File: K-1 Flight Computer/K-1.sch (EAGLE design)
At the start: 25 parts, among them IC1 BMP280, IC2 7805L, J1 1X2-3.5MM, J6 1X2-3.5MM, U1 MPU-6050-1, U2 W25Q32FV

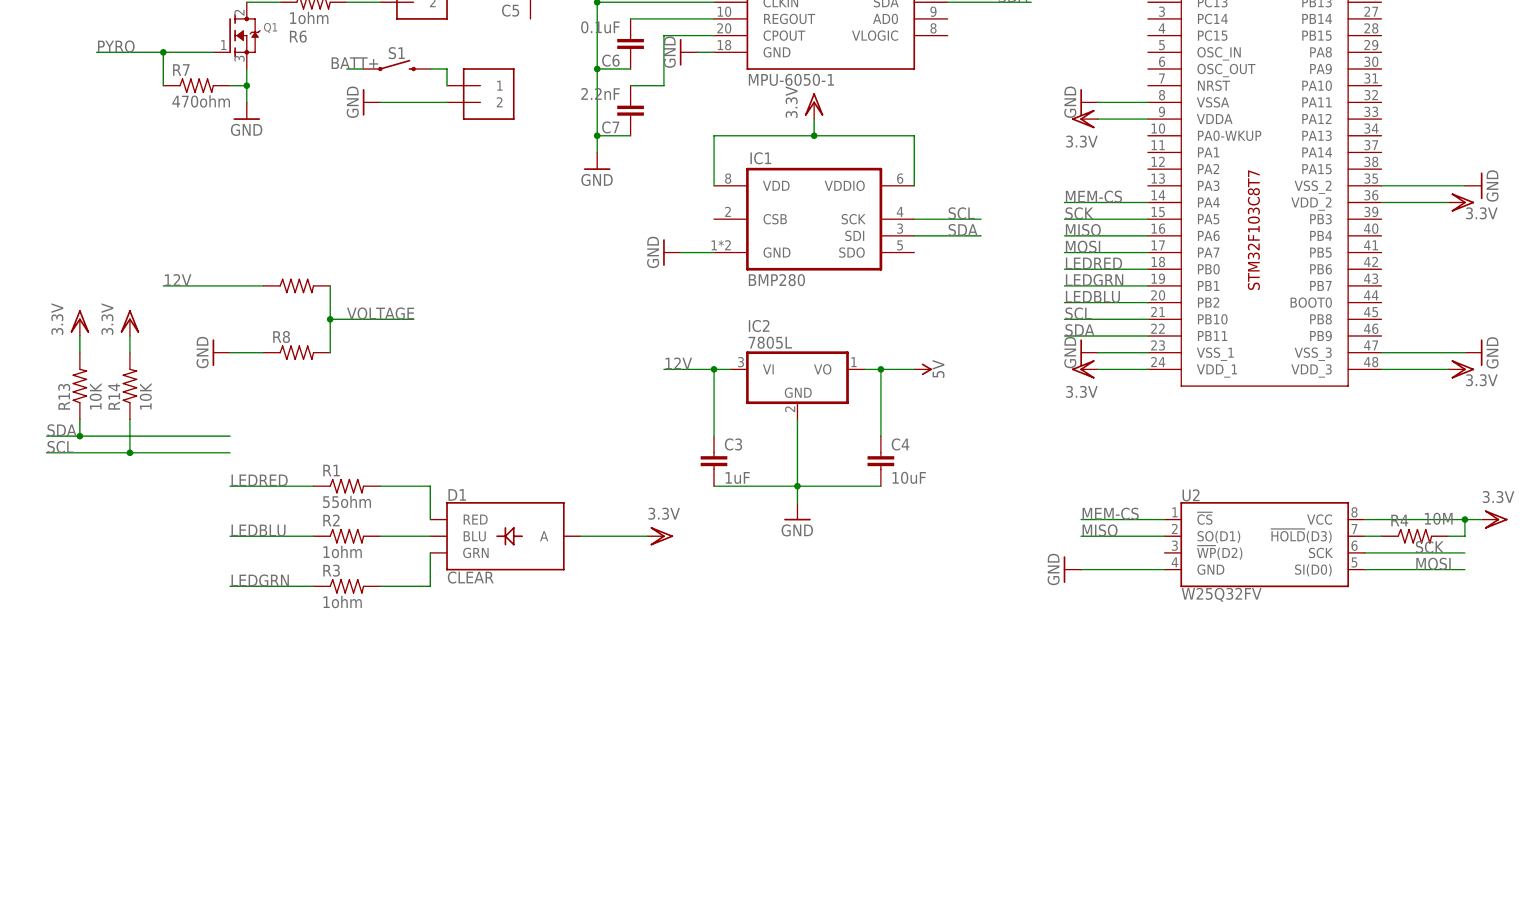
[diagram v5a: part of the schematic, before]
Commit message: completed bootloader circuit
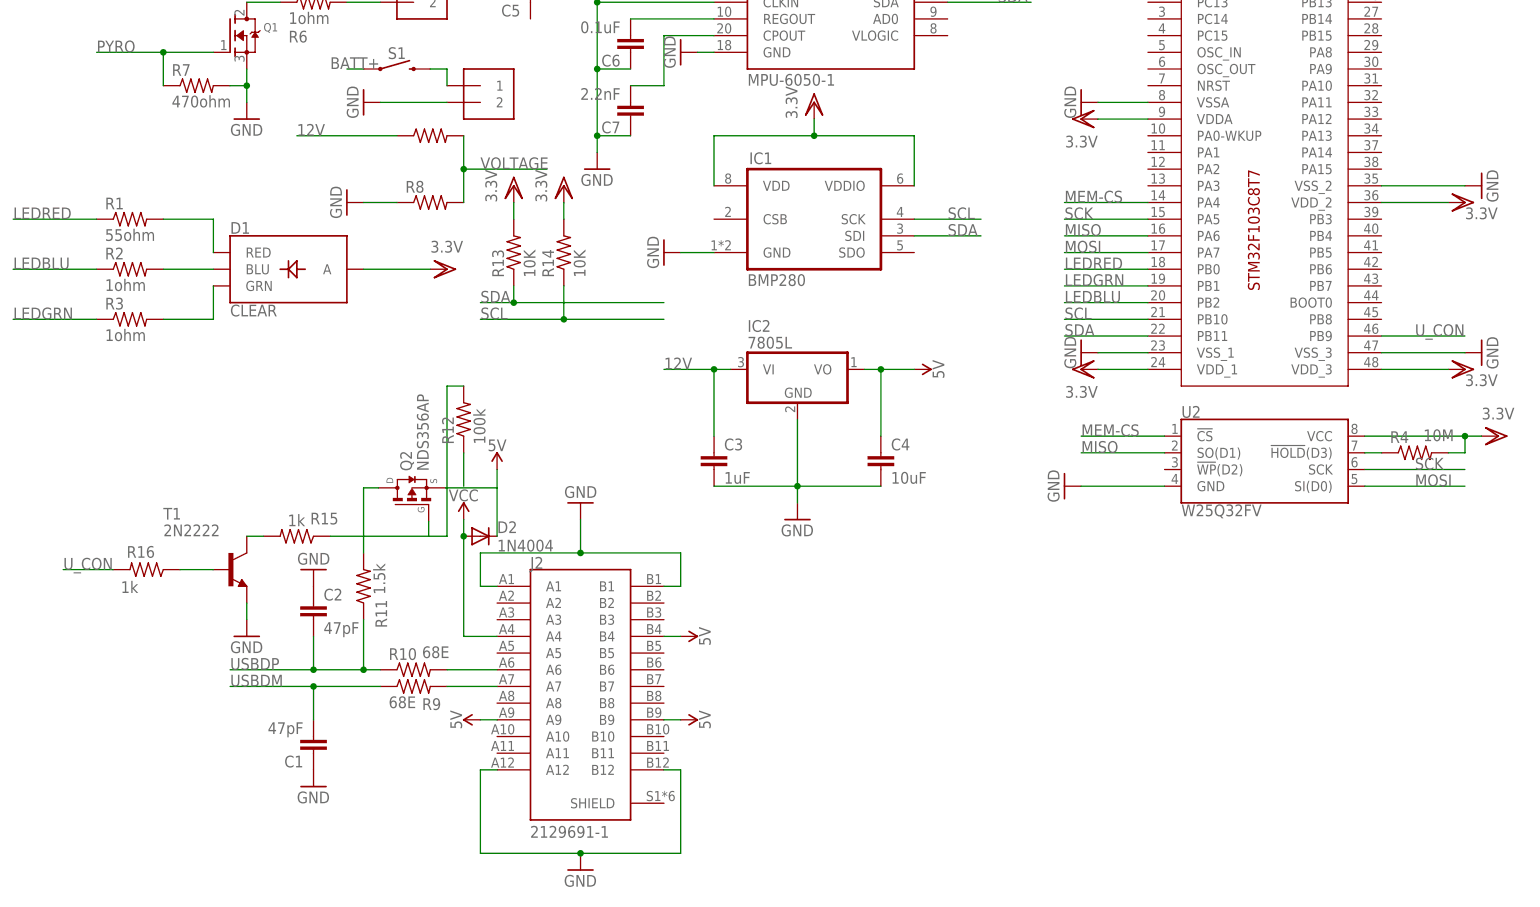
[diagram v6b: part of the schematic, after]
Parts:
- added C1, C2: 47pF, capacitor-wima:C2,5-3
- added D2: 1N4004, adafruit:1N4004
- added J2: 2129691-1, typeC:2129691-1
- added Q2: NDS356AP, NDS356AP:NDS356AP
- added R10, R9: 68E, adafruit:R-US_0204/2V
- added R11: 1.5k, adafruit:R-US_0204/2V
- added R12: 100k, adafruit:R-US_0204/2V
- added R15, R16: 1k, adafruit:R-US_0204/2V
- added T1: 2N2222, adafruit:2N2222
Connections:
- new net N$10: Q2.G, R12.2, R15.1
- new net N$13: R15.2, T1.C
- new net N$14: R16.1, T1.B
- new net N$16: J2.A7, R9.2
- new net N$7: J2.A6, R10.2
- new net N$8: Q2.D, R11.2
- new net N$9: R12.1
- new net USBDM: C1.2, R9.1
- new net USBDP: C2.2, R10.1, R11.1
- new net U_CON: R16.2, U$1.PB9
- new net VCC: D2.A, J2.A4
- net 5V: now also D2.C, J2.A9, J2.B4, J2.B9, Q2.S
- net GND: now also C1.1, C2.1, J2.A1, J2.A12, J2.B1, J2.B12, T1.E
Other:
- moved on the sheet: D1, R1, R13, R14, R2, R3, R4, R8, U2

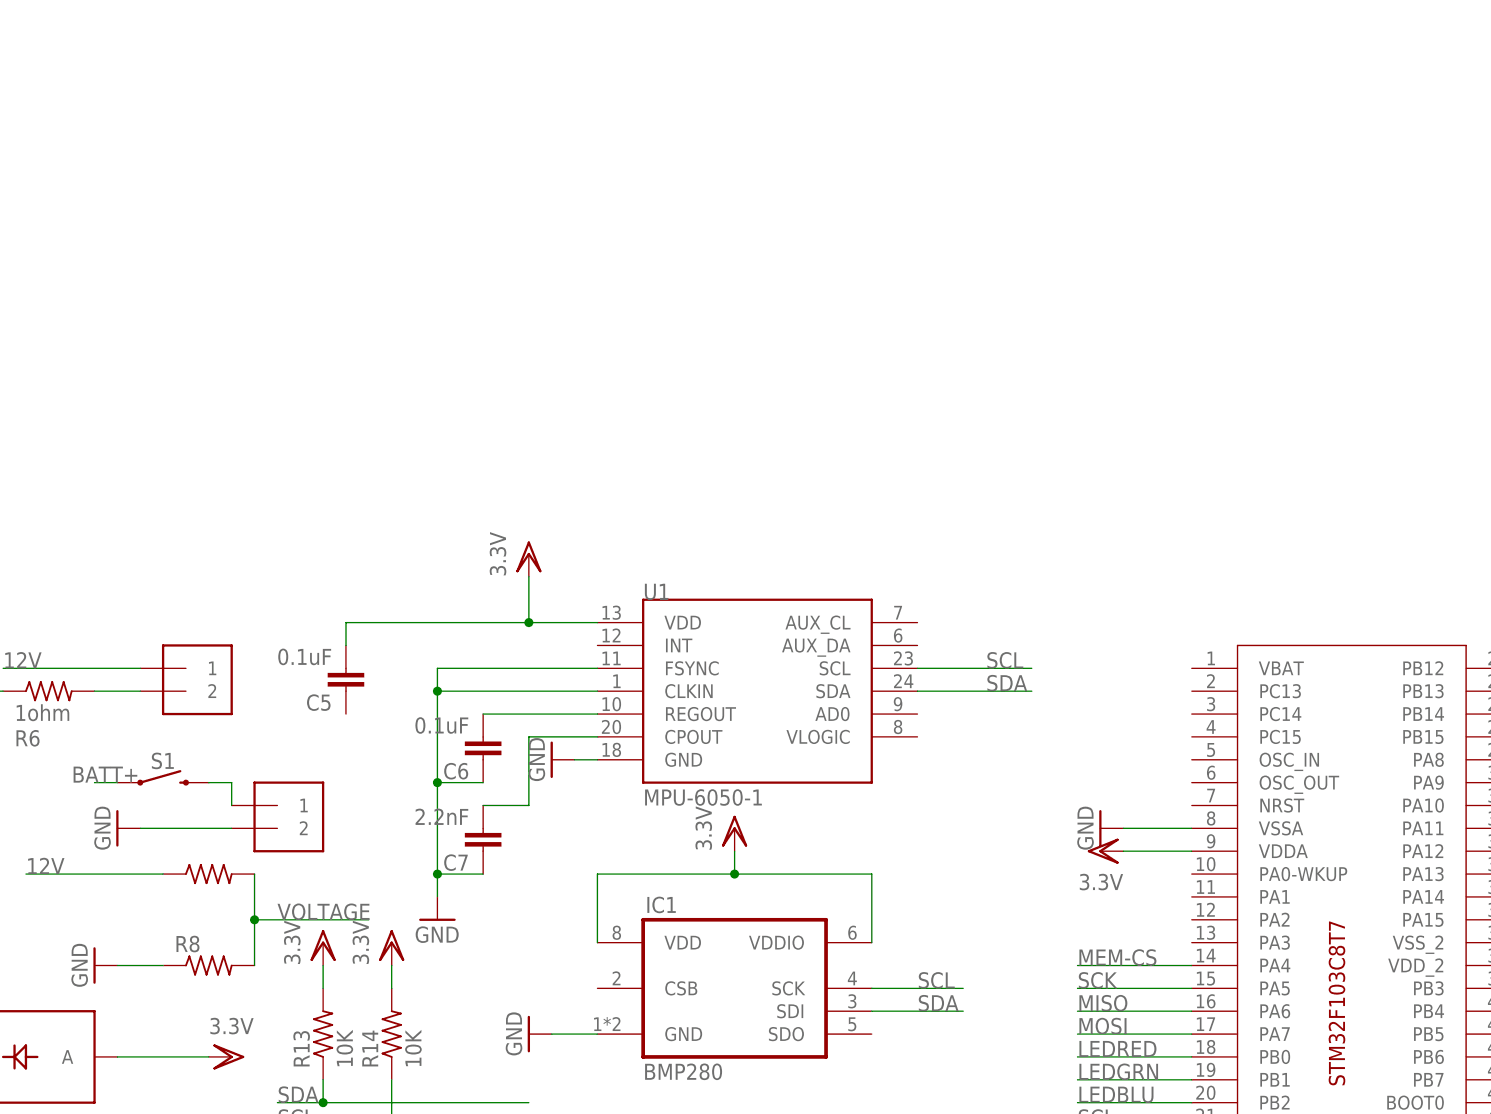
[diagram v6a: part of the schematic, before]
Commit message: completed IMU breakout circuit
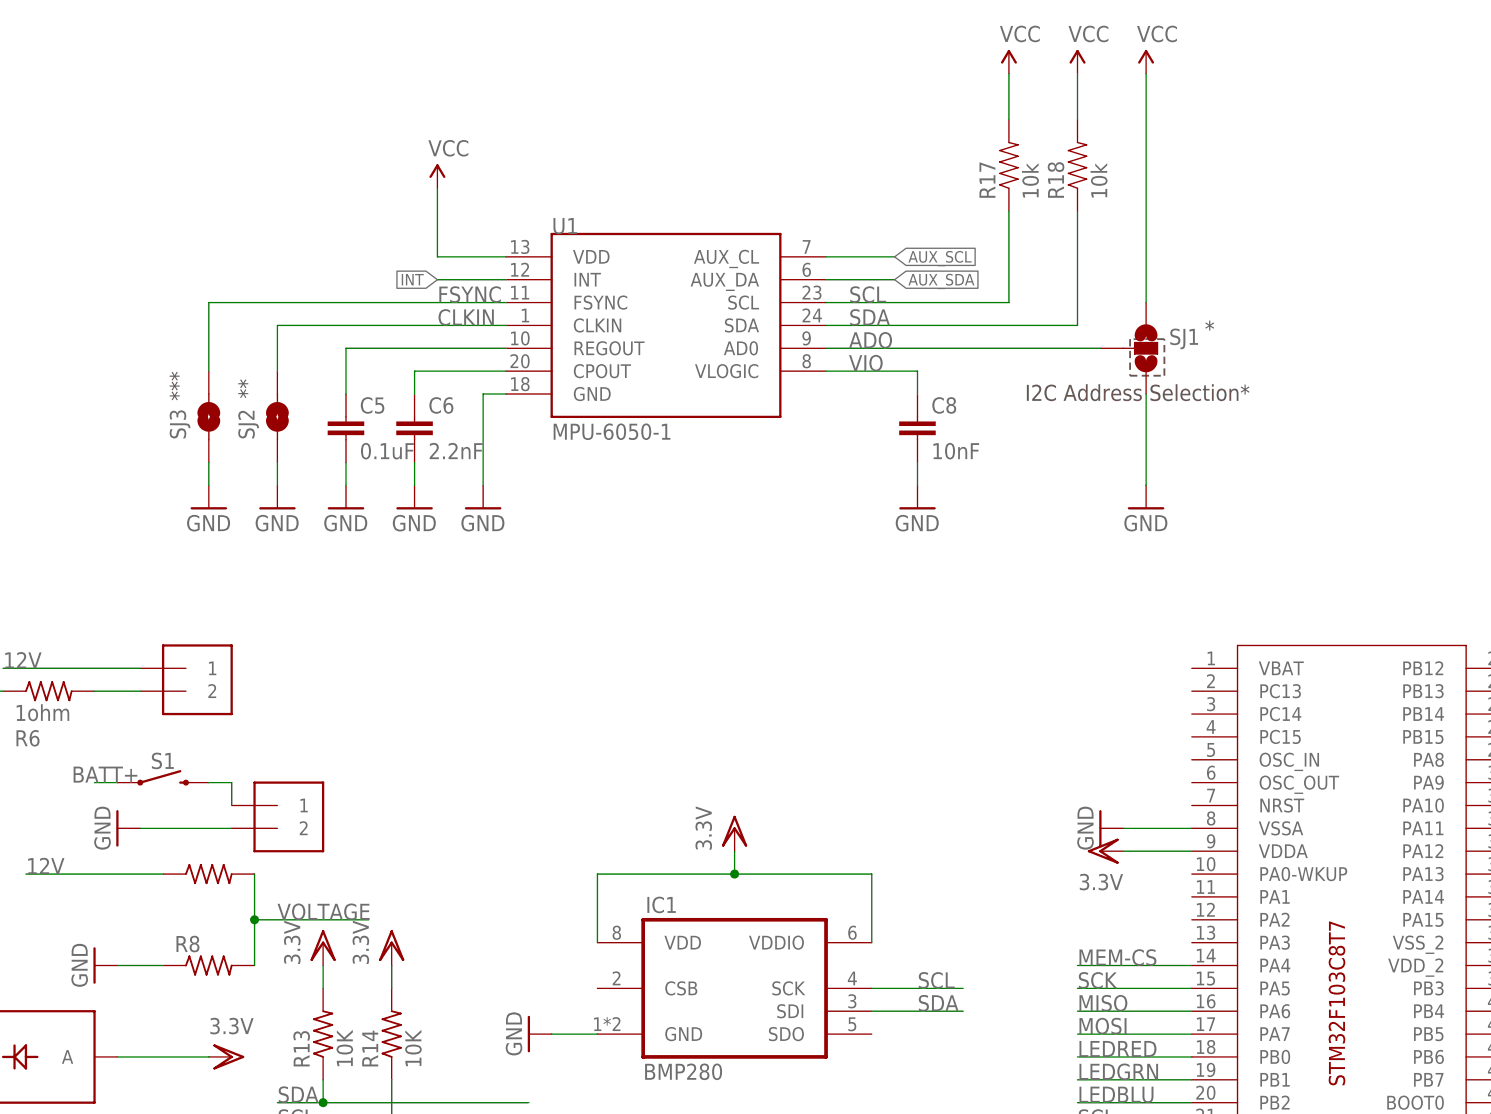
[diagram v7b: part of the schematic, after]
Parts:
- removed C7: 2.2nF, capacitor-wima:C2,5-3
- added C8: 10nF, SparkFun:CAP0603-CAP
- added R17, R18: 10k, SparkFun:RESISTOR0603-RES
- added SJ1: (no value), SparkFun:SOLDERJUMPER_2WAYPASTE2&3
- added SJ2, SJ3: SOLDERJUMPERTRACE, SparkFun:SOLDERJUMPERTRACE
- C5: device capacitor-wima:C2,5-3 -> SparkFun:CAP0603-CAP
- C6: value 0.1uF -> 2.2nF; device capacitor-wima:C2,5-3 -> SparkFun:CAP0603-CAP
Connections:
- new net ADO: SJ1.2, U1.AD0
- new net AUX_SCL: U1.AUX_CL
- new net AUX_SDA: U1.AUX_DA
- new net CLKIN: SJ2.2, U1.CLKIN
- new net FSYNC: SJ3.2, U1.FSYNC
- new net INT: U1.INT
- new net VIO: C8.1, U1.VLOGIC
- net GND: now also C5.2, C6.2, C8.2, SJ1.3, SJ2.1, SJ3.1; no longer C6.1, C7.1, U1.CLKIN, U1.FSYNC
- net N$11: now also C6.1; no longer C7.2
- net N$12: now also C5.1; no longer C6.2
- net SCL: now also R17.1
- net SDA: now also R18.1
- net VCC: now also R17.2, R18.2, SJ1.1, U1.VDD
- net VDD: no longer C5.2, U1.VDD
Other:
- note added: "*"
- note added: "**"
- note added: "***"
- note added: "I2C Address Selection*"
- moved on the sheet: C5, C6, U1
